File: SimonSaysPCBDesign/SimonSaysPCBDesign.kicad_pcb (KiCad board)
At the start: 2 copper layers, 36 parts, among them J1 Screw_Terminal, SW1 SW_SPST, SW2 SW_MEC_5E, SW3 SW_MEC_5E, SW4 SW_MEC_5E, SW6 SW_MEC_5E, U1 ATmega328P-P, U2 LM7805_TO220, U3 4-Pin I2C Header, Y1 16 Mhz

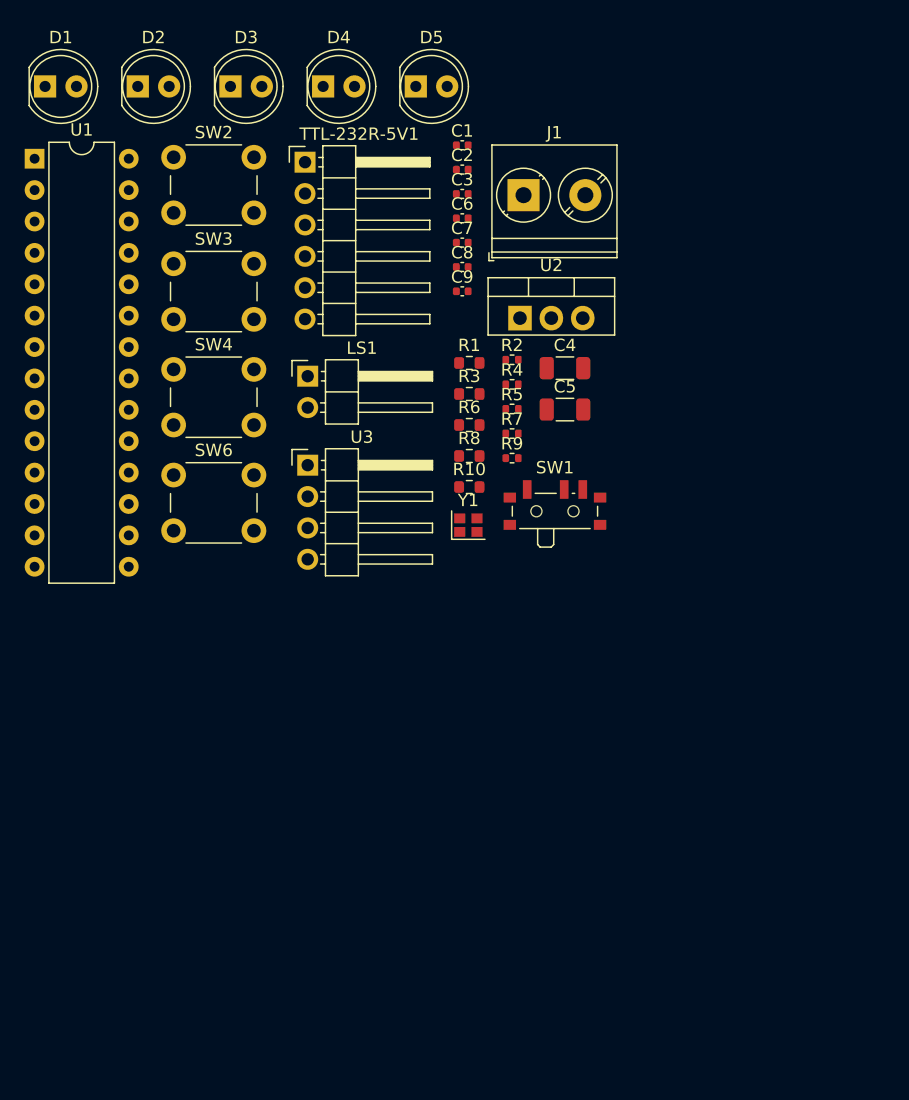
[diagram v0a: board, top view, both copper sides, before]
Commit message: Almost finished routing PCB
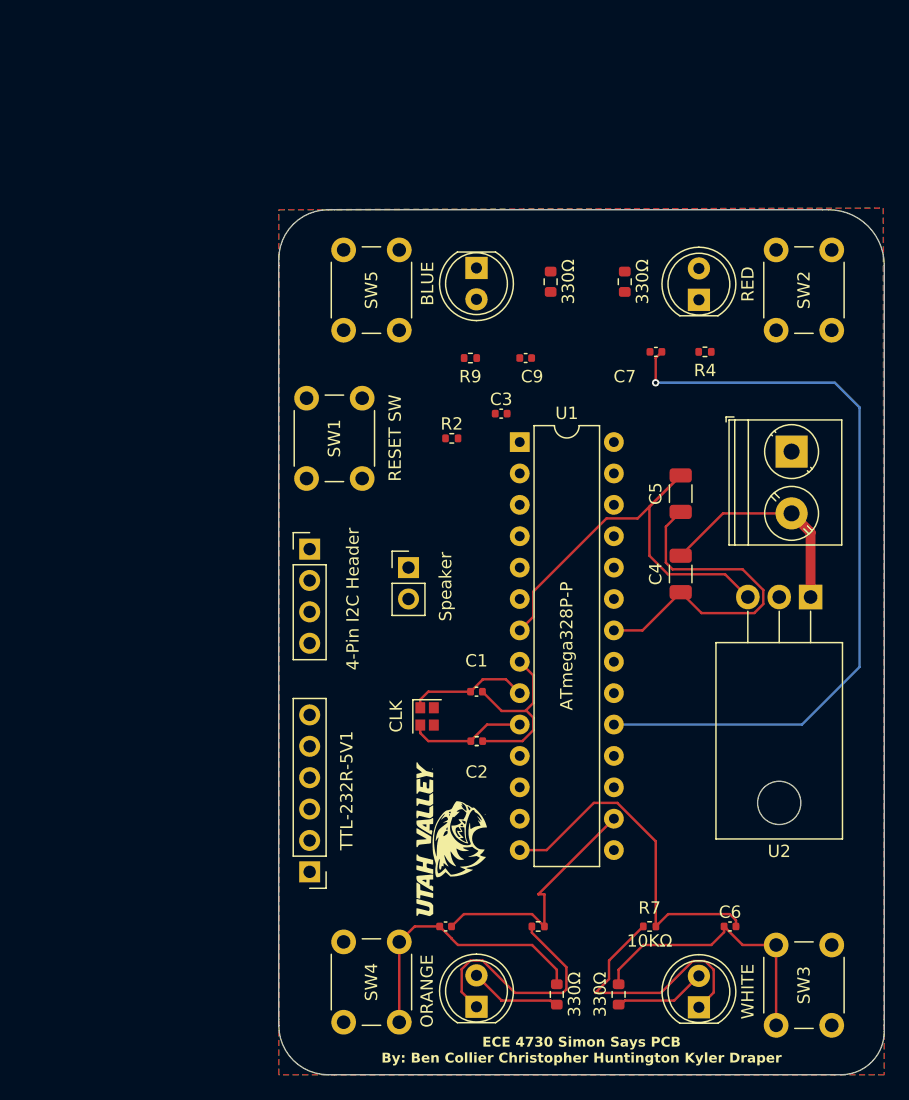
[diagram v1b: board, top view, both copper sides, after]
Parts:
- removed D1: RED, LED_THT:LED_D5.0mm
- removed R1: 220Ω, Resistor_SMD:R_0603_1608Metric
- removed SW6: SW_MEC_5E, Button_Switch_THT:SW_PUSH_6mm_H5mm
- added G***: LOGO, Logo Footprints:UVU, F.Cu at (122.5, 115.5)
- added SW5: SW_Push, Button_Switch_THT:SW_PUSH_6mm_H5mm, F.Cu at (113.8, 74.2)
- LS1: footprint Connector_PinHeader_2.54mm:PinHeader_1x02_P2.54mm_Horizontal -> Connector_PinHeader_2.54mm:PinHeader_1x02_P2.54mm_Vertical
- SW1: footprint Button_Switch_SMD:SW_SPDT_PCM12 -> Button_Switch_THT:SW_PUSH_6mm_H5mm
- SW2, SW3, SW4: value SW_MEC_5E -> SW_Push
- TTL-232R-5V1: footprint Connector_PinHeader_2.54mm:PinHeader_1x06_P2.54mm_Horizontal -> Connector_PinHeader_2.54mm:PinHeader_1x06_P2.54mm_Vertical
- U2: footprint Package_TO_SOT_THT:TO-220-3_Vertical -> Package_TO_SOT_THT:TO-220-3_Horizontal_TabDown
- U3: footprint Connector_PinHeader_2.54mm:PinHeader_1x04_P2.54mm_Horizontal -> Connector_PinHeader_2.54mm:PinHeader_1x04_P2.54mm_Vertical
- Y1: value 16 Mhz -> CLK
- moved D4 80.5 mm to (142.5, 129.0), turned to 90 degrees
- moved SW3 78.6 mm to (148.8, 130.5), turned to 90 degrees
- moved D3 77.1 mm to (124.5, 129.0), turned to 90 degrees
- moved C6 61.3 mm to (145.0, 122.5)
- moved TTL-232R-5V1 57.4 mm to (111.0, 118.1), turned to 180 degrees
- moved C8 53.4 mm to (122.0, 122.5)
- moved SW2 50.7 mm to (148.8, 74.2), turned to 90 degrees
- moved SW4 49.8 mm to (118.2, 123.8), turned to -90 degrees
- moved D2 48.6 mm to (142.5, 71.8), turned to 90 degrees
- moved R6 46.6 mm to (131.0, 128.0), turned to 90 degrees
- moved C2 46.3 mm to (124.5, 107.5)
- moved U1 45.5 mm to (128.0, 83.3)
- moved R8 45.2 mm to (136.0, 128.0), turned to 90 degrees
- moved C1 44.2 mm to (124.5, 103.5)
- moved R5 41.9 mm to (129.5, 122.5)
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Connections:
- C6 pad 1: Net-(SW3-A) -> Net-(C6-Pad1)
- C7 pad 1: Net-(SW2-A) -> Net-(C7-Pad1)
- C8 pad 1: Net-(SW4-A) -> Net-(C8-Pad1)
- C9 pad 1: Net-(SW6-A) -> Net-(C9-Pad1)
- R10 pad 2: Net-(SW6-K) -> Net-(C9-Pad1)
- R3 pad 2: Net-(SW2-K) -> Net-(C7-Pad1)
- R6 pad 2: Net-(SW4-K) -> Net-(C8-Pad1)
- R8 pad 2: Net-(SW3-K) -> Net-(C6-Pad1)
- SW2 pad 1: +5V -> Net-(C7-Pad1)
- SW2 pad 2: unconnected-(SW2-Pad2) -> +5V
- SW3 pad 1: +5V -> Net-(C6-Pad1)
- SW3 pad 2: unconnected-(SW3-Pad2) -> +5V
- SW4 pad 1: +5V -> Net-(C8-Pad1)
- SW4 pad 2: unconnected-(SW4-Pad2) -> +5V
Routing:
- net GND: track 0.00 -> 85.3 mm
- net Net-(U1-PB5): track 0.00 -> 62.9 mm, vias 0 -> 1
- net +5V: track 0.00 -> 36.3 mm
- net Net-(U1-PB0): track 0.00 -> 28.4 mm
- net Net-(C6-Pad1): track 0.00 -> 23.0 mm
- net Net-(C8-Pad1): track 0.00 -> 22.4 mm
- net Net-(U1-PB2): track 0.00 -> 20.1 mm
- net /+: track 0.00 -> 17.9 mm
- net XTAL1: track 0.00 -> 9.86 mm
- net XTAL2: track 0.00 -> 9.52 mm
- net Net-(D3-A): track 0.00 -> 7.50 mm
- net Net-(D4-A): track 0.00 -> 7.46 mm
- net Net-(D5-A): track 0.00 -> 0.85 mm
- added copper zone on F.Cu, net +5V
- added copper zone on B.Cu, net GND
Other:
- board outline added: 49 x 70 mm
- board text added: "ECE 4730 Simon Says PCB By: Ben Collier Christopher Huntington Kyler Draper"
- board text added: "RESET SW"

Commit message: Ran a few more traces
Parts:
- U3: value 4-Pin I2C Header -> I2C
- moved J1 4.54 mm to (149.0, 88.5), turned to 90 degrees
- moved G*** 1.58 mm to (121.0, 115.0)
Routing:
- net GND: track 85.3 -> 12.2 mm, vias 0 -> 8
- net Net-(SW1-B): track 0.00 -> 36.2 mm
- net Net-(U1-PD5): track 0.00 -> 23.4 mm
- net Net-(U1-PD2): track 0.00 -> 14.9 mm, vias 0 -> 1
- net /+: track 17.9 -> 26.4 mm
- net Net-(U1-~{RESET}/PC6): track 0.00 -> 3.12 mm

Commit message: Created Gerber Files
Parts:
- moved LS1 5.94 mm to (117.2, 99.1)
- moved G*** 1.12 mm to (120.0, 114.5)
- turned R10 to -90 degrees
- turned R3 to -90 degrees
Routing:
- net Net-(U1-PC4): track 0.00 -> 44.4 mm, vias 0 -> 1
- net Net-(TTL-232R-5V1-TXD): track 0.00 -> 36.2 mm, vias 0 -> 1
- net Net-(C9-Pad1): track 0.00 -> 35.2 mm
- net Net-(U1-PC5): track 0.00 -> 32.7 mm
- net Net-(TTL-232R-5V1-RXD): track 0.00 -> 30.2 mm
- net +5V: track 36.3 -> 11.4 mm, vias 0 -> 1
- net Net-(C7-Pad1): track 0.00 -> 23.1 mm
- net Net-(SW1-B): track 36.2 -> 43.7 mm
- net Net-(D2-A): track 0.00 -> 6.10 mm
- net Net-(D5-A): track 0.85 -> 6.93 mm
- net Net-(U1-PB5): track 62.9 -> 67.9 mm
- net Net-(U1-PD2): track 14.9 -> 19.9 mm
- net Net-(U1-PD5): track 23.4 -> 19.6 mm
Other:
- board text added: "PCB Version 1.0.0"
- board text added: "RESET"
- board text removed: "RESET SW"

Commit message: Added Gerber Files
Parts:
- moved LS1 4.77 mm to (121.0, 96.2)
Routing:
- net Net-(U1-PD5): track 19.6 -> 17.0 mm
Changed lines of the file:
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@@
 		(allow_soldermask_bridges_in_footprints no)
 		(pcbplotparams
-			(layerselection 0x00010fc_ffffffff)
+			(layerselection 0x003d0fc_ffffffff)
 			(plot_on_all_layers_selection 0x0000000_00000000)
 			(disableapertmacros no)
-			(usegerberextensions no)
-			(usegerberattributes yes)
-			(usegerberadvancedattributes yes)
+			(usegerberextensions yes)
+			(usegerberattributes no)
+			(usegerberadvancedattributes no)
 			(creategerberjobfile yes)
 			(dashed_line_dash_ratio 12.000000)
@@
 			(plotinvisibletext no)
 			(sketchpadsonfab no)
-			(subtractmaskfromsilk no)
+			(subtractmaskfromsilk yes)
 			(outputformat 1)
 			(mirror no)
-			(drillshape 1)
+			(drillshape 0)
 			(scaleselection 1)
-			(outputdirectory "")
+			(outputdirectory "../Gerber Files/")
 		)
 	)
@@
 		(tags "capacitor")
 		(property "Reference" "C5"
-			(at 0.275 -2.625 -90)
+			(at -0.025 -2.525 -90)
 			(layer "F.SilkS")
 			(effects
@@
 			(layer "F.Fab")
 		)
-		(fp_text user "${REFERENCE}"
-			(at 0 0 -90)
-			(layer "F.Fab")
-			(effects
-				(font
-					(size 0.8 0.8)
-					(thickness 0.12)
-				)
-			)
-		)
 		(pad "1" smd roundrect
 			(at -1.475 0 90)
 			(size 1.15 1.8)
 			(layers "F.Cu" "F.Paste" "F.Mask")
-			(roundrect_rratio 0.217391)
+			(roundrect_rratio 0.2173913043)
 			(net 2 "GND")
 			(pintype "passive")
@@
 			(size 1.15 1.8)
 			(layers "F.Cu" "F.Paste" "F.Mask")
-			(roundrect_rratio 0.217391)
+			(roundrect_rratio 0.2173913043)
 			(net 7 "+5V")
 			(pintype "passive")
@@
 		(tags "resistor")
 		(property "Reference" "R2"
-			(at 0 -1.17 0)
+			(at -1.01 1.75 0)
 			(layer "F.SilkS")
 			(effects
@@
 			(at 0 1.17 0)
 			(layer "F.Fab")
+			(hide yes)
 			(effects
 				(font
@@
 		(tags "capacitor")
 		(property "Reference" "C7"
-			(at -2.52 2 0)
+			(at -2.52 0.5 0)
 			(layer "F.SilkS")
 			(effects
@@
 		(tags "capacitor")
 		(property "Reference" "C3"
-			(at 0 -1.16 0)
+			(at 0.25 -2 0)
 			(layer "F.SilkS")
 			(effects
@@
 			(at 0 1.16 0)
 			(layer "F.Fab")
+			(hide yes)
 			(effects
 				(font
@@
 			(layer "F.Fab")
 		)
-		(fp_text user "${REFERENCE}"
-			(at 0 0 -90)
-			(layer "F.Fab")
-			(effects
-				(font
-					(size 0.8 0.8)
-					(thickness 0.12)
-				)
-			)
-		)
 		(pad "1" smd roundrect
 			(at -1.475 0 90)
 			(size 1.15 1.8)
 			(layers "F.Cu" "F.Paste" "F.Mask")
-			(roundrect_rratio 0.217391)
+			(roundrect_rratio 0.2173913043)
 			(net 2 "GND")
 			(pintype "passive")
@@
 			(size 1.15 1.8)
 			(layers "F.Cu" "F.Paste" "F.Mask")
-			(roundrect_rratio 0.217391)
+			(roundrect_rratio 0.2173913043)
 			(net 6 "/+")
 			(pintype "passive")
@@
 		(tags "capacitor")
 		(property "Reference" "C9"
-			(at 0.52 1.5 0)
+			(at 2.27 0.25 0)
 			(layer "F.SilkS")
 			(effects
@@
 			(layer "F.Fab")
 		)
-		(fp_text user "${REFERENCE}"
-			(at 1.25 0 90)
-			(layer "F.Fab")
-			(effects
-				(font
-					(size 0.8 0.8)
-					(thickness 0.2)
-				)
-			)
-		)
 		(pad "1" thru_hole rect
 			(at 0 0 270)
@@
 			(layer "F.Fab")
 		)
-		(fp_text user "${REFERENCE}"
-			(at 1.25 0 90)
-			(layer "F.Fab")
-			(effects
-				(font
-					(size 0.8 0.8)
-					(thickness 0.2)
-				)
-			)
-		)
 		(pad "1" thru_hole rect
 			(at 0 0 90)
@@
 			(at 2.54 -20.58 180)
 			(layer "F.SilkS")
+			(hide yes)
 			(effects
 				(font
@@
 		)
 		(property "Value" "LM7805_TO220"
-			(at 2.34 -2.96 180)
+			(at 2.54 -20.91 0)
 			(layer "F.Fab")
 			(effects
@@
 			(layer "F.Fab")
 		)
-		(fp_text user "${REFERENCE}"
-			(at 2.54 -20.58 180)
-			(layer "F.Fab")
-			(effects
-				(font
-					(size 1 1)
-					(thickness 0.15)
-				)
-			)
-		)
 		(pad "" np_thru_hole oval
 			(at 2.54 -16.66 180)
@@
 		)
 		(property "Value" "CLK"
-			(at 0 2.5 90)
+			(at 0.25 2.5 90)
 			(layer "F.SilkS")
 			(effects
@@
 		(tags "resistor")
 		(property "Reference" "R9"
-			(at -0.01 1.5 0)
+			(at -0.26 2 0)
 			(layer "F.SilkS")
 			(effects
@@
 			(layer "F.Fab")
 		)
-		(fp_text user "${REFERENCE}"
-			(at 1.25 0 -90)
-			(layer "F.Fab")
-			(effects
-				(font
-					(size 0.8 0.8)
-					(thickness 0.2)
-				)
-			)
-		)
 		(pad "1" thru_hole rect
 			(at 0 0 90)
@@
 	(footprint "Connector_PinHeader_2.54mm:PinHeader_1x02_P2.54mm_Vertical"
 		(layer "F.Cu")
-		(at 117.2 99.125)
+		(at 121 96.25)
 		(descr "Through hole straight pin header, 1x02, 2.54mm pitch, single row")
 		(tags "Through hole pin header THT 1x02 2.54mm single row")
@@
 		)
 		(property "Value" "Speaker"
-			(at 3 0.74 90)
+			(at -3 1 90)
 			(layer "F.SilkS")
 			(effects
@@
 			(layer "F.Fab")
 		)
-		(fp_text user "${REFERENCE}"
-			(at 0 1.27 90)
-			(layer "F.Fab")
-			(effects
-				(font
-					(size 1 1)
-					(thickness 0.15)
-				)
-			)
-		)
 		(pad "1" thru_hole rect
 			(at 0 0)
@@
 	)
 	(segment
-		(start 129.1 103.164365)
-		(end 128.455635 102.52)
+		(start 128 108.7)
+		(end 129.1 107.6)
 		(width 0.2)
 		(layer "F.Cu")
@@
 	)
 	(segment
-		(start 129.1 107.6)
-		(end 129.1 103.164365)
+		(start 121.274365 96.25)
+		(end 121 96.25)
 		(width 0.2)
 		(layer "F.Cu")
@@
 	)
 	(segment
-		(start 128.455635 102.52)
-		(end 127.544365 102.52)
+		(start 127.544365 102.52)
+		(end 121.274365 96.25)
 		(width 0.2)
 		(layer "F.Cu")
@@
 	)
 	(segment
-		(start 127.544365 102.52)
-		(end 124.149365 99.125)
+		(start 129.1 103.164365)
+		(end 128.455635 102.52)
 		(width 0.2)
 		(layer "F.Cu")
@@
 	)
 	(segment
-		(start 128 108.7)
-		(end 129.1 107.6)
+		(start 128.455635 102.52)
+		(end 127.544365 102.52)
 		(width 0.2)
 		(layer "F.Cu")
@@
 	)
 	(segment
-		(start 124.149365 99.125)
-		(end 117.2 99.125)
+		(start 129.1 107.6)
+		(end 129.1 103.164365)
 		(width 0.2)
 		(layer "F.Cu")
